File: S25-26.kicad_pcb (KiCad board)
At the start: 6 copper layers, 90 x 90 mm, 122 parts, among them IC1 CMV4000-3E5M0PN, IC10 DS90LV048ATM_NOPB, IC2 MXL86110I-AQB-R, IC3 NCV317BD2TR4G, IC4 MT29F2G01ABAGDWB-IT_G_TR, IC5 MT29F2G01ABAGDWB-IT_G_TR, IC6 XMC7200D-E272K8384AA, IC7 DS90LV011AHMF_NOPB, IC8 DS90LV048ATM_NOPB, IC9 DS90LV048ATM_NOPB, J1 DC_IN_PADS, J2 Conn_01x04_Pin, J3 Conn_01x02_Pin, J4 RJ45_RB1-125B8G1A, Q1 ZXT849K, U1 TPS73601MDRBREP, U2 TPS73601MDRBREP, Y1 DSC1101DM2-012.0000

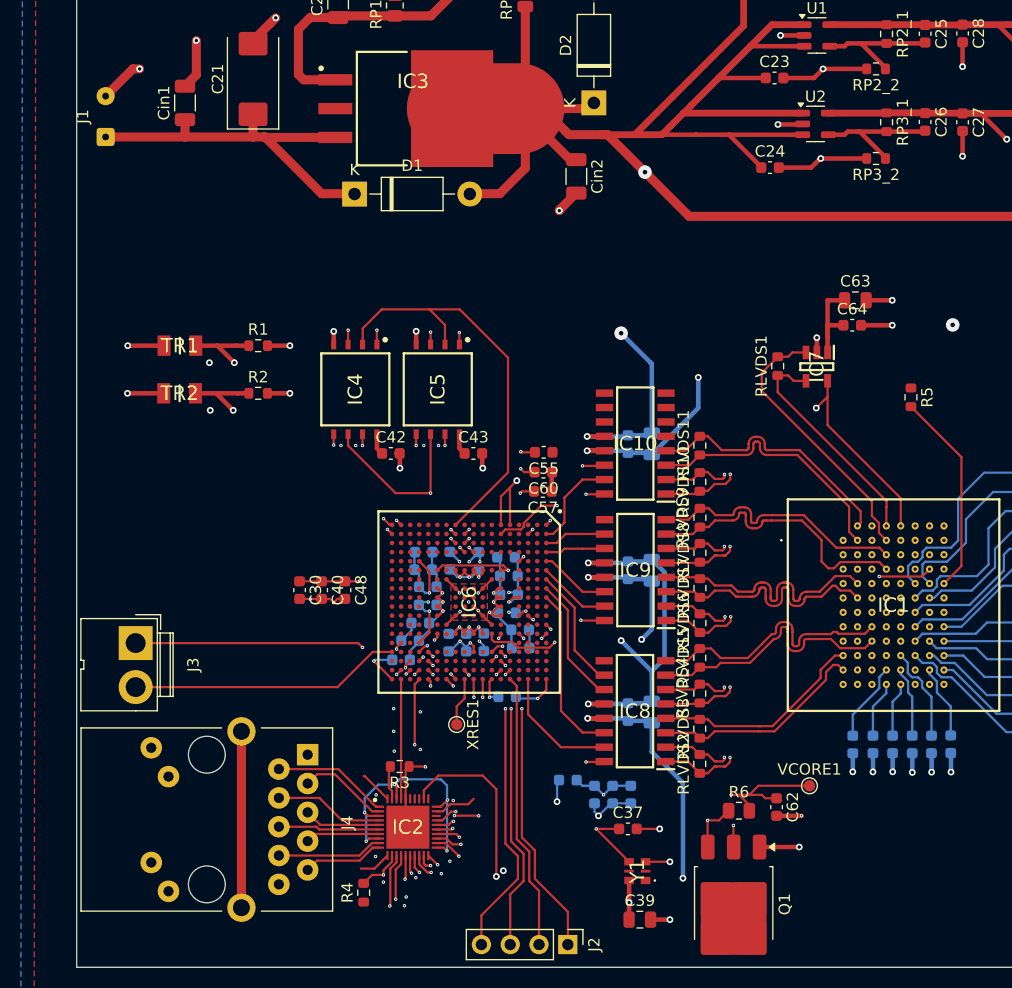
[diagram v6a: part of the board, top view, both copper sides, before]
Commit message: Testpads everywhere; passives' footprints updated from MDE components; bigger DC_IN pads
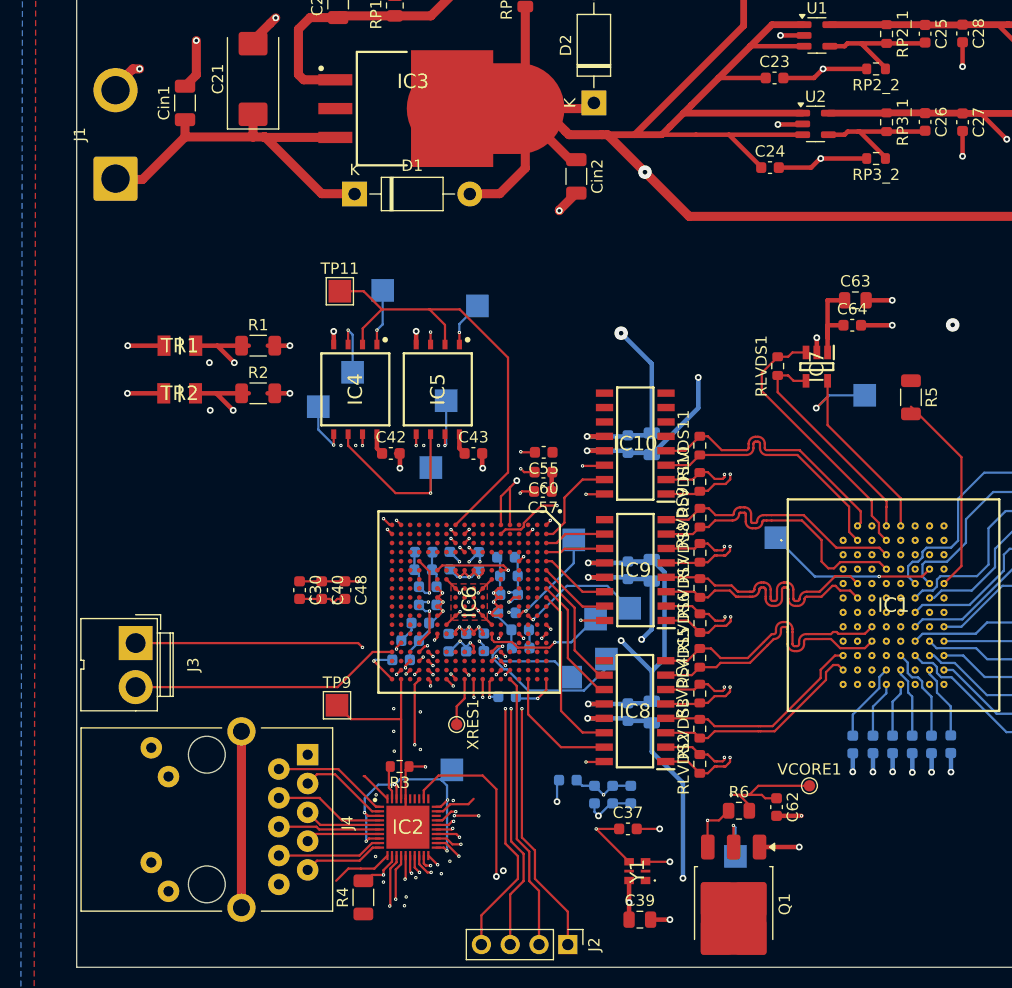
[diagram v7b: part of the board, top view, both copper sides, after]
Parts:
- added TP1: CMOS_RESET_N, TestPoint:TestPoint_Pad_2.0x2.0mm, B.Cu at (154.2, 109.5)
- added TP10: QSPI_SEL0, TestPoint:TestPoint_Pad_2.0x2.0mm, B.Cu at (135.4, 80.5)
- added TP11: QSPI_IO1, TestPoint:TestPoint_Pad_2.0x2.0mm, F.Cu at (131.6, 80.6)
- added TP12: QSPI_IO2, TestPoint:TestPoint_Pad_2.0x2.0mm, B.Cu at (132.7, 87.8)
- added TP13: QSPI_IO3, TestPoint:TestPoint_Pad_2.0x2.0mm, B.Cu at (141.0, 90.2)
- added TP14: QSPI_SCLK, TestPoint:TestPoint_Pad_2.0x2.0mm, B.Cu at (139.6, 96.2)
- added TP15: QSPI_IO0, TestPoint:TestPoint_Pad_2.0x2.0mm, B.Cu at (129.7, 90.8)
- added TP16: DRV_VOUT, TestPoint:TestPoint_Pad_2.0x2.0mm, B.Cu at (166.5, 130.4)
- added TP17: QSPI_SEL1, TestPoint:TestPoint_Pad_2.0x2.0mm, B.Cu at (143.7, 81.9)
- added TP2: CMOS_SPI_CLK, TestPoint:TestPoint_Pad_2.0x2.0mm, B.Cu at (157.2, 108.5)
- added TP3: CMOS_SPI_EN, TestPoint:TestPoint_Pad_2.0x2.0mm, B.Cu at (170.1, 102.3)
- added TP4: FRAME_REQ, TestPoint:TestPoint_Pad_2.0x2.0mm, B.Cu at (152.2, 102.5)
- added TP5: CMOS_SPI_MOSI, TestPoint:TestPoint_Pad_2.0x2.0mm, B.Cu at (155.1, 113.0)
- added TP6: CMOS_SPI_MISO, TestPoint:TestPoint_Pad_2.0x2.0mm, B.Cu at (151.9, 114.6)
- added TP7: CMOS_MASTER_CLK, TestPoint:TestPoint_Pad_2.0x2.0mm, B.Cu at (177.9, 89.8)
- added TP8: VDD1V1, TestPoint:TestPoint_Pad_2.0x2.0mm, B.Cu at (141.5, 122.8)
- added TP9: ETH0_REF_CLK, TestPoint:TestPoint_Pad_2.0x2.0mm, F.Cu at (131.3, 117.1)
- J1: footprint Connector_Wire:SolderWire-0.1sqmm_1x02_P3.6mm_D0.4mm_OD1mm -> Connector_Wire:SolderWire-2sqmm_1x02_P7.8mm_D2mm_OD3.9mm
- R1, R2, R4, R5: footprint Resistor_SMD:R_0603_1608Metric -> Resistor_SMD:R_1206_3216Metric
- moved J1 3.78 mm to (111.8, 70.7)
- moved R4 0.41 mm to (133.7, 134.0)
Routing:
- net /CMOS_SPI_MOSI: track 67.4 -> 81.7 mm
- net /CMOS_RESET_N: track 59.6 -> 70.1 mm
- net /CMOS_SPI_EN: track 41.8 -> 52.3 mm
- net /FRAME_REQ: track 43.7 -> 51.7 mm
- net /CMOS_SPI_MISO: track 64.2 -> 71.5 mm
- net /ETH0_REF_CLK: track 10.6 -> 16.8 mm
- net /CMOS_MASTER_CLK: track 53.7 -> 58.4 mm
- net /Processing/QSPI_IO1: track 37.0 -> 41.4 mm
- net /CMOS_SPI_CLK: track 58.2 -> 62.6 mm
- net /Processing/QSPI_IO3: track 21.8 -> 25.7 mm
- net /Processing/QSPI_IO0: track 31.6 -> 35.5 mm
- net /Processing/QSPI_IO2: track 31.4 -> 35.3 mm
- net /Processing/QSPI_SEL0: track 22.8 -> 26.5 mm
- net /Processing/QSPI_SEL1: track 20.6 -> 23.6 mm
- net /Processing/DRV_VOUT: track 31.2 -> 34.0 mm
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
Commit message: Final Changes before Order
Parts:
- moved C59 1.34 mm to (135.7, 113.1)
- moved C46 1.12 mm to (136.7, 111.4)
- moved C34 0.11 mm to (146.2, 109.0)
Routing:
- net +3V3: track 538.6 -> 543.4 mm
- net GND: track 553.8 -> 549.8 mm, vias 101 -> 95
- net /CMOS_RESET_N: track 70.1 -> 71.5 mm
- net /CMOS_SPI_MOSI: track 81.7 -> 82.4 mm
- net /CMOS_SPI_CLK: track 62.6 -> 62.4 mm, vias 1 -> 2
- net /CMOS_SPI_EN: track 52.3 -> 52.4 mm, vias 2 -> 4
- removed copper zone on In4.Cu, net +3V3
